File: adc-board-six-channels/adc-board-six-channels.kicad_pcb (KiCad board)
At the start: 2 copper layers, 35 x 44.5 mm, 44 parts, among them J1 Conn_02x08_Odd_Even, J2 Conn_02x08_Odd_Even, U1 ADC_SPI_GEN, U2 ADC_SPI_GEN, U3 ADC_SPI_GEN, U4 ADC_SPI_GEN, U5 ADC_SPI_GEN, U6 ADC_SPI_GEN

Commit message: Updated boards with dates, silk, mounting holes
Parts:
- added REF**: MountingHole_3.2mm_M3, MountingHole:MountingHole_3.2mm_M3, F.Cu at (107.1, 55.7)
- added REF**: MountingHole_3.2mm_M3, MountingHole:MountingHole_3.2mm_M3, F.Cu at (107.1, 19.3)
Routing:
- net GND: vias 6 -> 11
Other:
- board text added: "3V3"
- board text added: "5V"
- board text added: "A1"
- board text added: "A2"
- board text added: "A3"
- board text added: "A4"
- board text added: "A5"
- board text added: "A6"
- board text added: "CLK"
- board text added: "SD1"
- board text added: "SD2"
- board text added: "SD3/ ~CS"
- board text added: "SD4/ CLK"
- board text added: "SD5"
- board text added: "SD6"
- board text added: "Vcc"
- board text added: "~CS"
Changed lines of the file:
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@@
     (property "Sheetname" "")
     (attr through_hole)
-    (fp_text reference "J1" (at 4.6415 20.1526) (layer "F.SilkS")
-      (effects (font (size 1 1) (thickness 0.15)))
+    (fp_text reference "J1" (at -1.17695 20.1422) (layer "F.SilkS")
+      (effects (font (size 0.7 0.7) (thickness 0.15)))
     )
     (fp_text value "Conn_02x08_Odd_Even" (at 5.655 20.05) (layer "F.Fab")
@@
     (attr through_hole)
     (fp_text reference "J2" (at 4.724 -2.2756) (layer "F.SilkS")
-      (effects (font (size 1 1) (thickness 0.15)))
+      (effects (font (size 0.7 0.7) (thickness 0.15)))
     )
     (fp_text value "Conn_02x08_Odd_Even" (at 5.655 20.05) (layer "F.Fab")
@@
     )
   )
+  (footprint "MountingHole:MountingHole_3.2mm_M3" (layer "F.Cu")
+    (at 107.0864 55.7022)
+    (descr "Mounting Hole 3.2mm, no annular, M3")
+    (tags "mounting hole 3.2mm no annular m3")
+    (attr exclude_from_pos_files exclude_from_bom)
+    (fp_text reference "REF**" (at 0 -4.2) (layer "F.SilkS") hide
+      (effects (font (size 1 1) (thickness 0.15)))
+    )
+    (fp_text value "MountingHole_3.2mm_M3" (at 0 4.2) (layer "F.Fab")
+      (effects (font (size 1 1) (thickness 0.15)))
+    )
+    (fp_text user "${REFERENCE}" (at 0 0) (layer "F.Fab")
+      (effects (font (size 1 1) (thickness 0.15)))
+    )
+    (fp_circle (center 0 0) (end 3.2 0) (layer "Cmts.User") (width 0.15) (fill none))
+    (fp_circle (center 0 0) (end 3.45 0) (layer "F.CrtYd") (width 0.05) (fill none))
+    (pad "" np_thru_hole circle (at 0 0) (size 3.2 3.2) (drill 3.2) (layers *.Cu *.Mask))
+  )
   (footprint "Capacitor_SMD:C_0805_2012Metric_Pad1.18x1.45mm_HandSolder" (layer "F.Cu")
     (at 89.97695 27.202 90)
@@
     )
   )
+  (footprint "MountingHole:MountingHole_3.2mm_M3" (layer "F.Cu")
+    (at 107.1372 19.2786)
+    (descr "Mounting Hole 3.2mm, no annular, M3")
+    (tags "mounting hole 3.2mm no annular m3")
+    (attr exclude_from_pos_files exclude_from_bom)
+    (fp_text reference "REF**" (at 0 -4.2) (layer "F.SilkS") hide
+      (effects (font (size 1 1) (thickness 0.15)))
+    )
+    (fp_text value "MountingHole_3.2mm_M3" (at 0 4.2) (layer "F.Fab")
+      (effects (font (size 1 1) (thickness 0.15)))
+    )
+    (fp_text user "${REFERENCE}" (at 0 0) (layer "F.Fab")
+      (effects (font (size 1 1) (thickness 0.15)))
+    )
+    (fp_circle (center 0 0) (end 3.2 0) (layer "Cmts.User") (width 0.15) (fill none))
+    (fp_circle (center 0 0) (end 3.45 0) (layer "F.CrtYd") (width 0.05) (fill none))
+    (pad "" np_thru_hole circle (at 0 0) (size 3.2 3.2) (drill 3.2) (layers *.Cu *.Mask))
+  )
   (footprint "Resistor_SMD:R_0805_2012Metric_Pad1.20x1.40mm_HandSolder" (layer "B.Cu")
     (at 88.96795 21.63)
@@
   )
   (gr_rect (start 75.26045 15.2296) (end 110.26045 59.7296) (layer "Edge.Cuts") (width 0.1) (fill none))
-  (gr_text "Six-channel ADC board\nv1.0 - 08.2022" (at 96.9772 57.5056) (layer "F.SilkS")
+  (gr_text "A2\n" (at 84.5312 31.115) (layer "F.SilkS")
+    (effects (font (size 0.7 0.7) (thickness 0.175)))
+  )
+  (gr_text "~CS" (at 96.4184 29.9974) (layer "F.SilkS")
+    (effects (font (size 0.7 0.7) (thickness 0.175)))
+  )
+  (gr_text "SD4/\nCLK" (at 100.7364 36.6522) (layer "F.SilkS")
+    (effects (font (size 0.7 0.7) (thickness 0.175)))
+  )
+  (gr_text "A3\n" (at 84.5058 33.8074) (layer "F.SilkS")
+    (effects (font (size 0.7 0.7) (thickness 0.175)))
+  )
+  (gr_text "Vcc" (at 82.7024 53.5686) (layer "F.SilkS")
+    (effects (font (size 0.7 0.7) (thickness 0.175)))
+  )
+  (gr_text "5V" (at 84.7344 46.4312) (layer "F.SilkS")
+    (effects (font (size 0.7 0.7) (thickness 0.175)))
+  )
+  (gr_text "Six-channel ADC board\nv1.0 - 08.2022" (at 83.058 57.2262) (layer "F.SilkS")
     (effects (font (size 0.7 0.7) (thickness 0.15)) (justify left))
+  )
+  (gr_text "A5" (at 84.455 38.735) (layer "F.SilkS")
+    (effects (font (size 0.7 0.7) (thickness 0.175)))
+  )
+  (gr_text "A1" (at 84.455 28.4734) (layer "F.SilkS")
+    (effects (font (size 0.7 0.7) (thickness 0.175)))
+  )
+  (gr_text "CLK" (at 96.5454 35.8394) (layer "F.SilkS")
+    (effects (font (size 0.7 0.7) (thickness 0.175)))
+  )
+  (gr_text "A6" (at 84.5312 41.4528) (layer "F.SilkS")
+    (effects (font (size 0.7 0.7) (thickness 0.175)))
+  )
+  (gr_text "3V3" (at 84.7598 43.7896) (layer "F.SilkS")
+    (effects (font (size 0.7 0.7) (thickness 0.175)))
+  )
+  (gr_text "SD1" (at 100.7618 28.6512) (layer "F.SilkS")
+    (effects (font (size 0.7 0.7) (thickness 0.175)))
+  )
+  (gr_text "SD2" (at 100.6856 31.115) (layer "F.SilkS")
+    (effects (font (size 0.7 0.7) (thickness 0.175)))
+  )
+  (gr_text "SD3/\n~CS" (at 100.7618 33.8074) (layer "F.SilkS")
+    (effects (font (size 0.7 0.7) (thickness 0.175)))
+  )
+  (gr_text "5V" (at 100.4824 46.4566) (layer "F.SilkS")
+    (effects (font (size 0.7 0.7) (thickness 0.175)))
+  )
+  (gr_text "3V3" (at 100.5586 43.942) (layer "F.SilkS")
+    (effects (font (size 0.7 0.7) (thickness 0.175)))
+  )
+  (gr_text "SD5" (at 100.6856 38.8112) (layer "F.SilkS")
+    (effects (font (size 0.7 0.7) (thickness 0.175)))
+  )
+  (gr_text "A4" (at 84.5566 36.322) (layer "F.SilkS")
+    (effects (font (size 0.7 0.7) (thickness 0.175)))
+  )
+  (gr_text "SD6" (at 100.711 41.4274) (layer "F.SilkS")
+    (effects (font (size 0.7 0.7) (thickness 0.175)))
   )
   (segment (start 87.376 45.085) (end 87.63 45.339) (width 0.35) (layer "F.Cu") (net 1))
@@
   (segment (start 79.9592 56.6928) (end 80.7212 56.6928) (width 0.35) (layer "B.Cu") (net 1))
   (segment (start 86.93895 49.47395) (end 86.93895 46.03005) (width 0.35) (layer "B.Cu") (net 1))
+  (via (at 95.4532 50.4952) (size 0.8) (drill 0.4) (layers "F.Cu" "B.Cu") (free) (net 2))
   (via (at 89.96495 45.8874) (size 0.8) (drill 0.4) (layers "F.Cu" "B.Cu") (net 2))
   (via (at 89.98395 39.267) (size 0.8) (drill 0.4) (layers "F.Cu" "B.Cu") (net 2))
@@
   (via (at 89.98395 52.602) (size 0.8) (drill 0.4) (layers "F.Cu" "B.Cu") (net 2))
   (via (at 89.98395 26.112) (size 0.8) (drill 0.4) (layers "F.Cu" "B.Cu") (net 2))
+  (via (at 95.3262 37.0078) (size 0.8) (drill 0.4) (layers "F.Cu" "B.Cu") (free) (net 2))
+  (via (at 95.3262 24.003) (size 0.8) (drill 0.4) (layers "F.Cu" "B.Cu") (free) (net 2))
+  (via (at 94.488 29.6418) (size 0.8) (drill 0.4) (layers "F.Cu" "B.Cu") (free) (net 2))
+  (via (at 95.3008 43.307) (size 0.8) (drill 0.4) (layers "F.Cu" "B.Cu") (free) (net 2))
   (via (at 89.98395 19.508) (size 0.8) (drill 0.4) (layers "F.Cu" "B.Cu") (net 2))
   (segment (start 92.01445 21.548) (end 90.06445 21.548) (width 0.254) (layer "F.Cu") (net 3))
@@
   (segment (start 87.94895 34.7364) (end 86.86755 33.655) (width 0.254) (layer "B.Cu") (net 15))
   (segment (start 86.86755 33.655) (end 81.90645 33.655) (width 0.254) (layer "B.Cu") (net 15))
-  (segment (start 84.78705 28.2344) (end 85.13895 28.2344) (width 0.254) (layer "F.Cu") (net 16))
-  (segment (start 81.90645 31.115) (end 84.78705 28.2344) (width 0.254) (layer "F.Cu") (net 16))
-  (via (at 85.13895 28.2344) (size 0.8) (drill 0.4) (layers "F.Cu" "B.Cu") (net 16))
-  (segment (start 85.13935 28.234) (end 85.13895 28.2344) (width 0.254) (layer "B.Cu") (net 16))
-  (segment (start 87.96795 28.234) (end 85.13935 28.234) (width 0.254) (layer "B.Cu") (net 16))
+  (segment (start 85.6488 28.2194) (end 84.80205 28.2194) (width 0.254) (layer "F.Cu") (net 16))
+  (segment (start 84.80205 28.2194) (end 81.90645 31.115) (width 0.254) (layer "F.Cu") (net 16))
+  (via (at 85.6488 28.2194) (size 0.8) (drill 0.4) (layers "F.Cu" "B.Cu") (net 16))
+  (segment (start 85.6488 28.2194) (end 85.6634 28.234) (width 0.254) (layer "B.Cu") (net 16))
+  (segment (start 85.6634 28.234) (end 87.96795 28.234) (width 0.254) (layer "B.Cu") (net 16))
   (segment (start 85.13895 21.6304) (end 81.90645 24.8629) (width 0.254) (layer "F.Cu") (net 17))
   (segment (start 81.90645 24.8629) (end 81.90645 28.575) (width 0.254) (layer "F.Cu") (net 17))

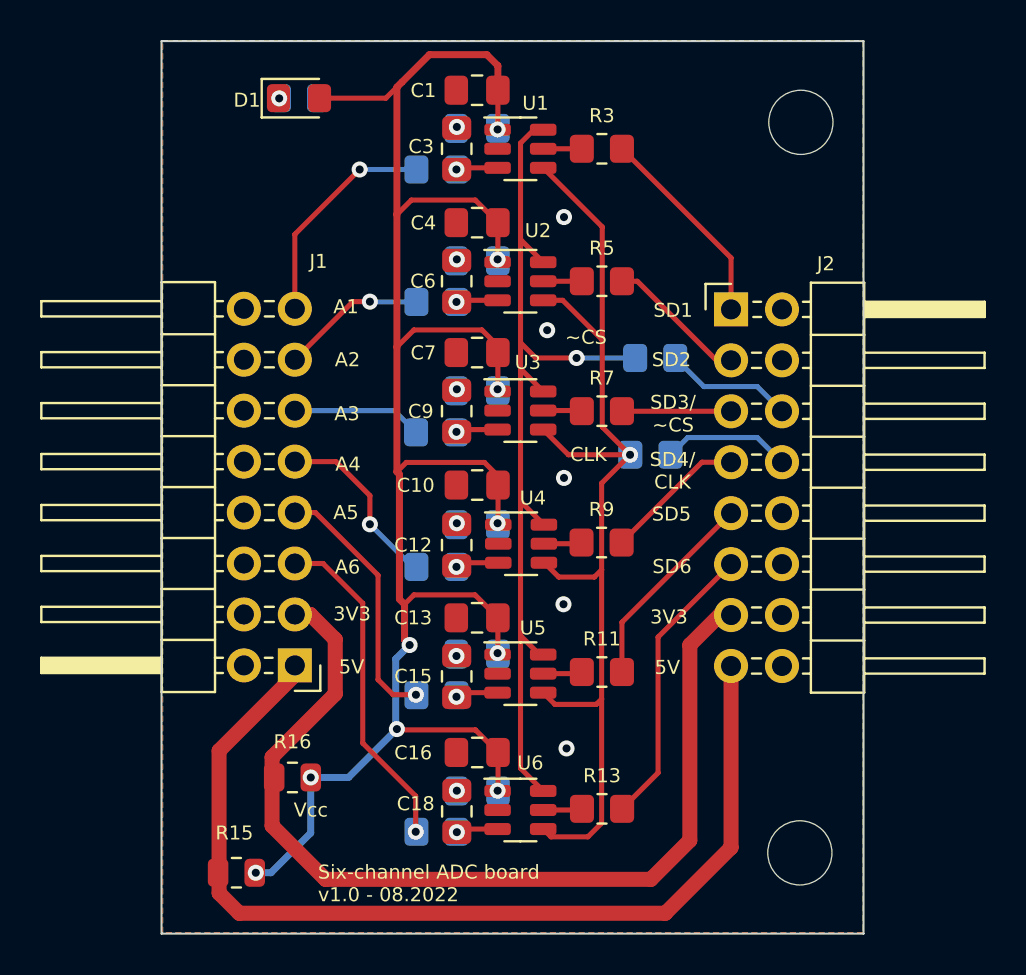
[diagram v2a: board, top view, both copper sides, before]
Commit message: Generated gerber files for adc-fiber-interface board
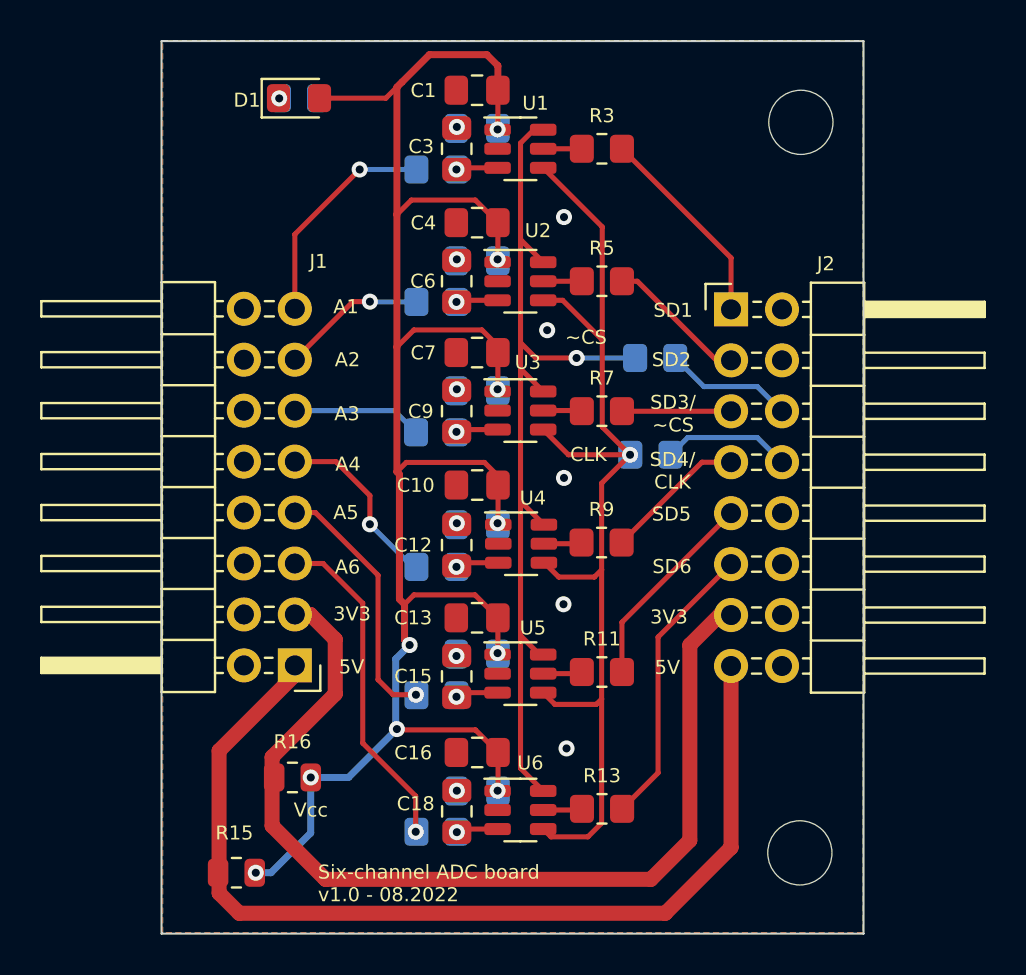
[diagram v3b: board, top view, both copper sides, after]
